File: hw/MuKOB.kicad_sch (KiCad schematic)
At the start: 135 parts, among them J1 UART0 IO01, J10 IO_EX, J11 SPKR_L, J12 SPKR_R, J13 UI 20-RBN, J14 AUDIO, J15 SPI-0, J16 SPI-DISP, J17 SW_MATRIX, J18 UIM 20-FCC, J19 UIM 20-RBN, J2 SERIAL-COMM, J3 KEY_SND_IF, J4 GPIO28, J5 I2C-0, J6 MicroSD-Socket w/Det, J7 KEY-PADDLE, J8 UART1 IO89, J9 UI 20-FCC, Q1 2N3904, SW1 RESET, SW2 RE-SO, SW3 UP, SW4 LF, SW5 EN, SW6 RT, SW7 DN, SW8 RE-AO, SW9 RE-BO, U1 MAX3221, U2 PicoW, U3 MCP23S08-E/SO, U4 TLV70033_SOT23-5, U5 TPA2012D2RTJT, U6 NC7WZ16P6X

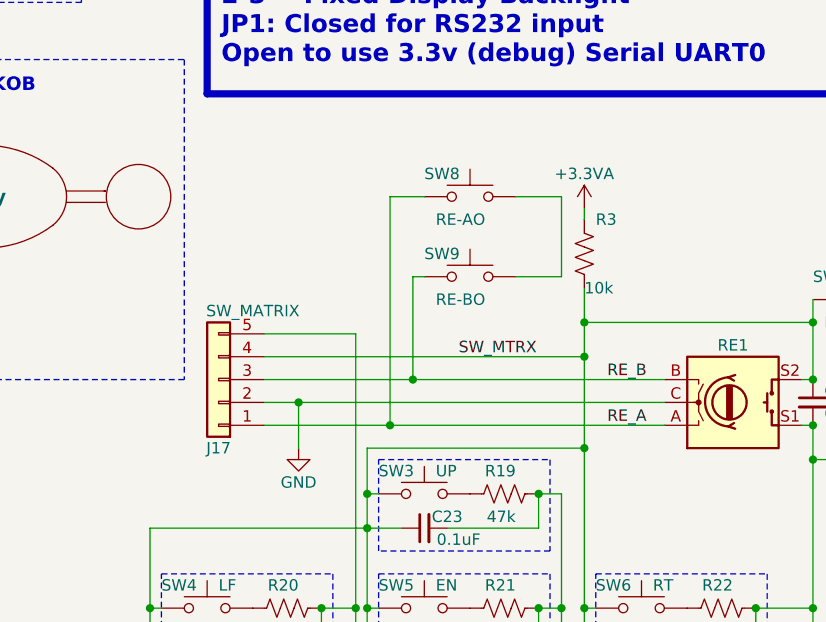
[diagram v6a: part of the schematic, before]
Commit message: Add 3D components for rendering.
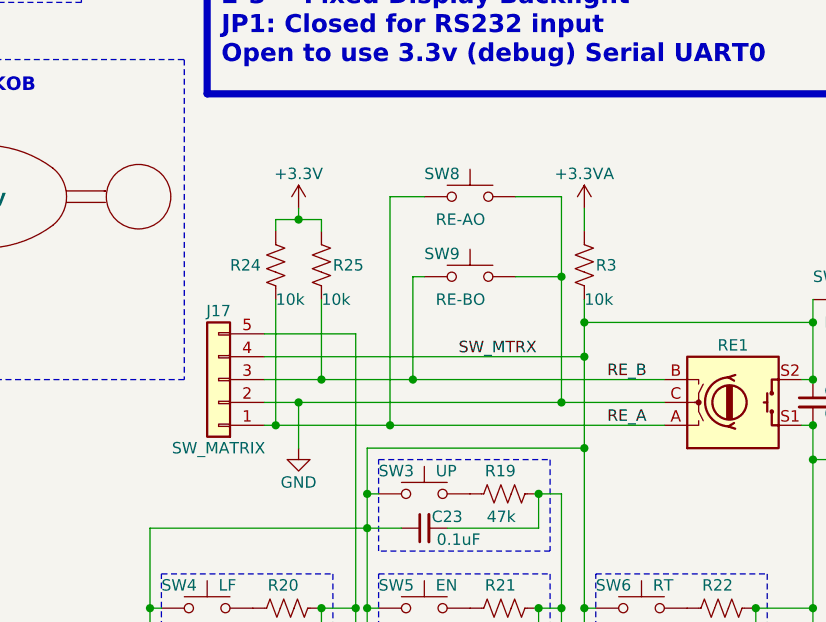
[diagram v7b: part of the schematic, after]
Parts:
- added R24, R25: 10k, Resistor_SMD:R_0402_1005Metric_Pad0.72x0.64mm_HandSolder, symbol Device:R_US
- J15, J3: footprint Connector_PinHeader_2.54mm:PinHeader_1x07_P2.54mm_Vertical -> Connector_PinSocket_2.54mm:PinSocket_1x07_P2.54mm_Vertical
- TP1, TP2, TP3, TP4, TP5: footprint Connector_PinSocket_2.54mm:PinSocket_1x01_P2.54mm_Vertical -> Connector_PinHeader_2.54mm:PinHeader_1x01_P2.54mm_Vertical
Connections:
- net +3.3V: now also R24.1, R25.1
- net GND: now also SW8.2, SW9.2
- net RE_A: now also R24.2
- net RE_B: now also R25.2
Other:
- moved on the sheet: R3
